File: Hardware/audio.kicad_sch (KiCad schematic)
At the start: 17 parts, among them J8 Conn_01x03, U4 LP5907MFX-3.3, U5 PCM5100

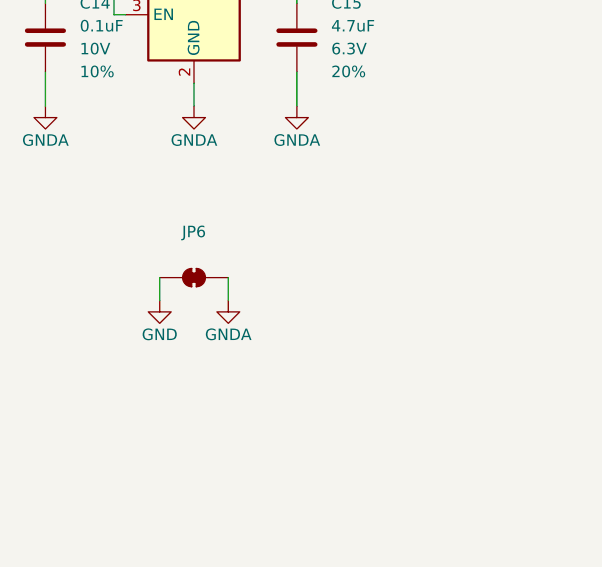
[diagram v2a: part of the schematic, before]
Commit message: Update all jumper names to match labels.
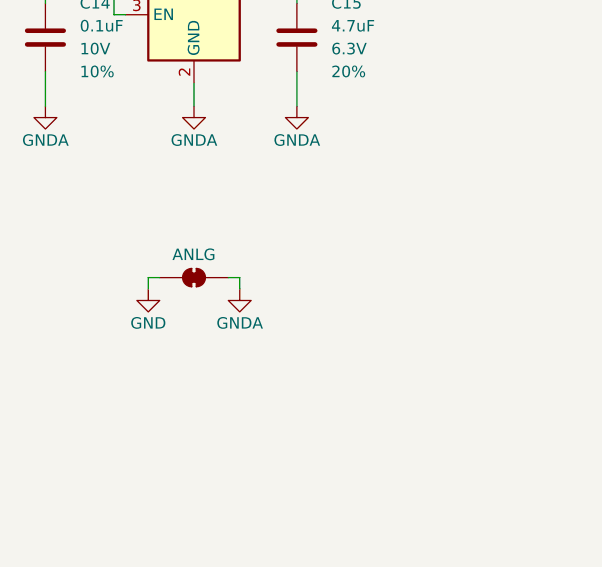
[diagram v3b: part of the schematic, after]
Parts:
- JP6: value ~ -> ANLG
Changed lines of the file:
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@@
-	(wire
-		(pts
-			(xy 59.69 113.03) (xy 59.69 115.57)
-		)
-		(stroke
-			(width 0)
-			(type default)
-		)
-	)
 	(wire
 		(pts
@@
 	(wire
 		(pts
-			(xy 52.07 113.03) (xy 52.07 115.57)
+			(xy 50.8 113.03) (xy 50.8 114.3)
 		)
 		(stroke
@@
 	(wire
 		(pts
+			(xy 60.96 113.03) (xy 60.96 114.3)
+		)
+		(stroke
+			(width 0)
+			(type default)
+		)
+	)
+	(wire
+		(pts
 			(xy 204.47 83.82) (xy 217.17 83.82)
 		)
@@
 	(wire
 		(pts
+			(xy 60.96 113.03) (xy 59.69 113.03)
+		)
+		(stroke
+			(width 0)
+			(type default)
+		)
+	)
+	(wire
+		(pts
 			(xy 124.46 95.25) (xy 124.46 93.98)
 		)
@@
 		(pts
 			(xy 39.37 81.28) (xy 39.37 82.55)
+		)
+		(stroke
+			(width 0)
+			(type default)
+		)
+	)
+	(wire
+		(pts
+			(xy 50.8 113.03) (xy 52.07 113.03)
 		)
 		(stroke
@@
 	(symbol
 		(lib_id "power:GNDA")
-		(at 59.69 115.57 0)
+		(at 60.96 114.3 0)
 		(unit 1)
 		(exclude_from_sim no)
@@
 		(dnp no)
 		(property "Reference" "#PWR078"
-			(at 59.69 121.92 0)
+			(at 60.96 120.65 0)
 			(effects
 				(font
@@
 		)
 		(property "Value" "GNDA"
-			(at 59.69 119.38 0)
+			(at 60.96 118.11 0)
 			(effects
 				(font
@@
 		)
 		(property "Footprint" ""
-			(at 59.69 115.57 0)
+			(at 60.96 114.3 0)
 			(effects
 				(font
@@
 		)
 		(property "Datasheet" ""
-			(at 59.69 115.57 0)
+			(at 60.96 114.3 0)
 			(effects
 				(font
@@
 		)
 		(property "Description" "Power symbol creates a global label with name \"GNDA\" , analog ground"
-			(at 59.69 115.57 0)
+			(at 60.96 114.3 0)
 			(effects
 				(font
@@
 	(symbol
 		(lib_id "SparkFun-PowerSymbol:GND")
-		(at 52.07 115.57 0)
+		(at 50.8 114.3 0)
 		(unit 1)
 		(exclude_from_sim no)
@@
 		(dnp no)
 		(property "Reference" "#PWR077"
-			(at 52.07 121.92 0)
+			(at 50.8 120.65 0)
 			(effects
 				(font
@@
 		)
 		(property "Value" "GND"
-			(at 52.07 119.38 0)
+			(at 50.8 118.11 0)
 			(do_not_autoplace yes)
 			(effects
@@
 		)
 		(property "Footprint" ""
-			(at 52.07 115.57 0)
+			(at 50.8 114.3 0)
 			(effects
 				(font
@@
 		)
 		(property "Datasheet" ""
-			(at 52.07 115.57 0)
+			(at 50.8 114.3 0)
 			(effects
 				(font
@@
 		)
 		(property "Description" "Power symbol creates a global label with name \"GND\" , ground"
-			(at 52.07 115.57 0)
+			(at 50.8 114.3 0)
 			(effects
 				(font
@@
 					(size 1.27 1.27)
 				)
-			)
-		)
-		(property "Value" "~"
+				(hide yes)
+			)
+		)
+		(property "Value" "ANLG"
 			(at 55.88 110.49 0)
 			(effects

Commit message: Update parts to use SparkFun lib. Update PCB to v10 copper.
Resolve ERC and DRC issues.
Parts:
- U4: symbol Qwiic_Turntable_Unique_Parts:LP5907MFX-3.3 -> SparkFun-Regulator:LP5907MFX-3.3
- U5: symbol Qwiic_Turntable_Unique_Parts:PCM5100 -> SparkFun-IC-Special-Function:PCM5100
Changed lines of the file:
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@@
 	)
 	(symbol
-		(lib_id "Qwiic_Turntable_Unique_Parts:LP5907MFX-3.3")
+		(lib_id "SparkFun-Regulator:LP5907MFX-3.3")
 		(at 55.88 83.82 0)
 		(unit 1)
@@
 	)
 	(symbol
-		(lib_id "Qwiic_Turntable_Unique_Parts:PCM5100")
+		(lib_id "SparkFun-IC-Special-Function:PCM5100")
 		(at 182.88 93.98 0)
 		(unit 1)
